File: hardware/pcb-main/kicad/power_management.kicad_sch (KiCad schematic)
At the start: 58 parts, among them J7 TYPE-C-31-M-12, J8 JST_PH_2pin, Q2 PMOS, SW1 SS-12D10L5, U5 BQ24195RGER, U6 TPS61088RHLR, U7 INA219AIDCNR, U8 AMS1117-3.3, U9 USBLC6-2SC6

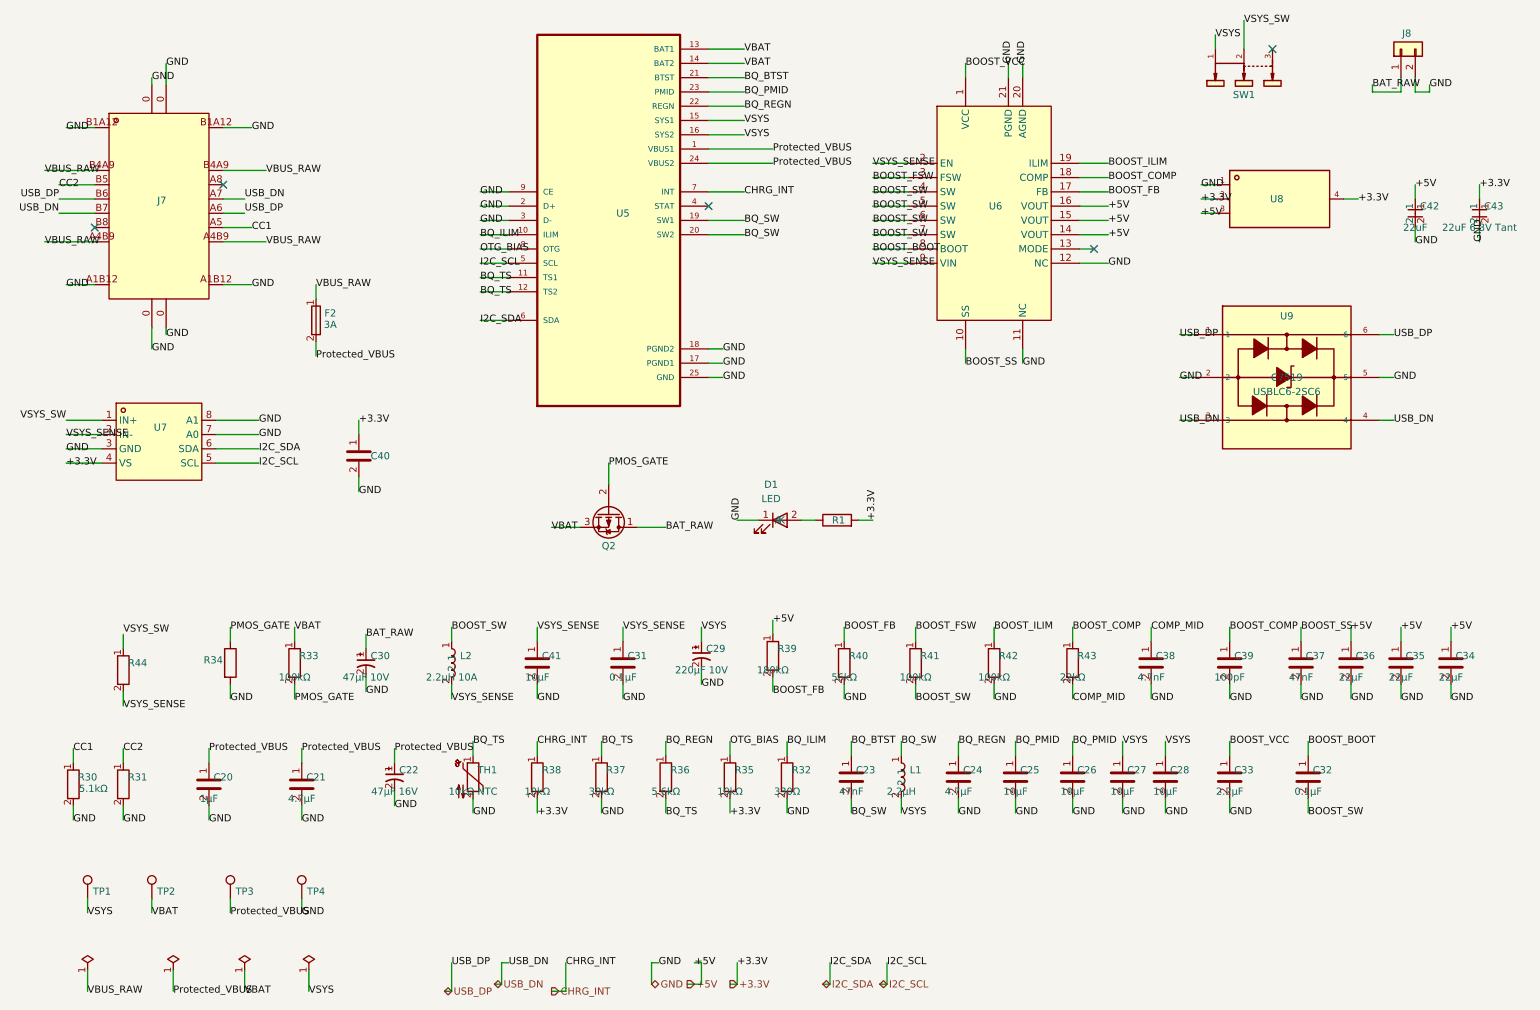
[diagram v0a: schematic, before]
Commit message: Main PCB v7 finalization: schematic, layout, production files, and reports
Includes power management schematic updates, PCB layout changes,
updated BOM/positions/netlist for JLCPCB fabrication, DRC/ERC reports,
slide switch footprint library addition, and review handoff docs.

Co-Authored-By: Claude Opus 4.6 (1M context) <noreply@anthropic.com>
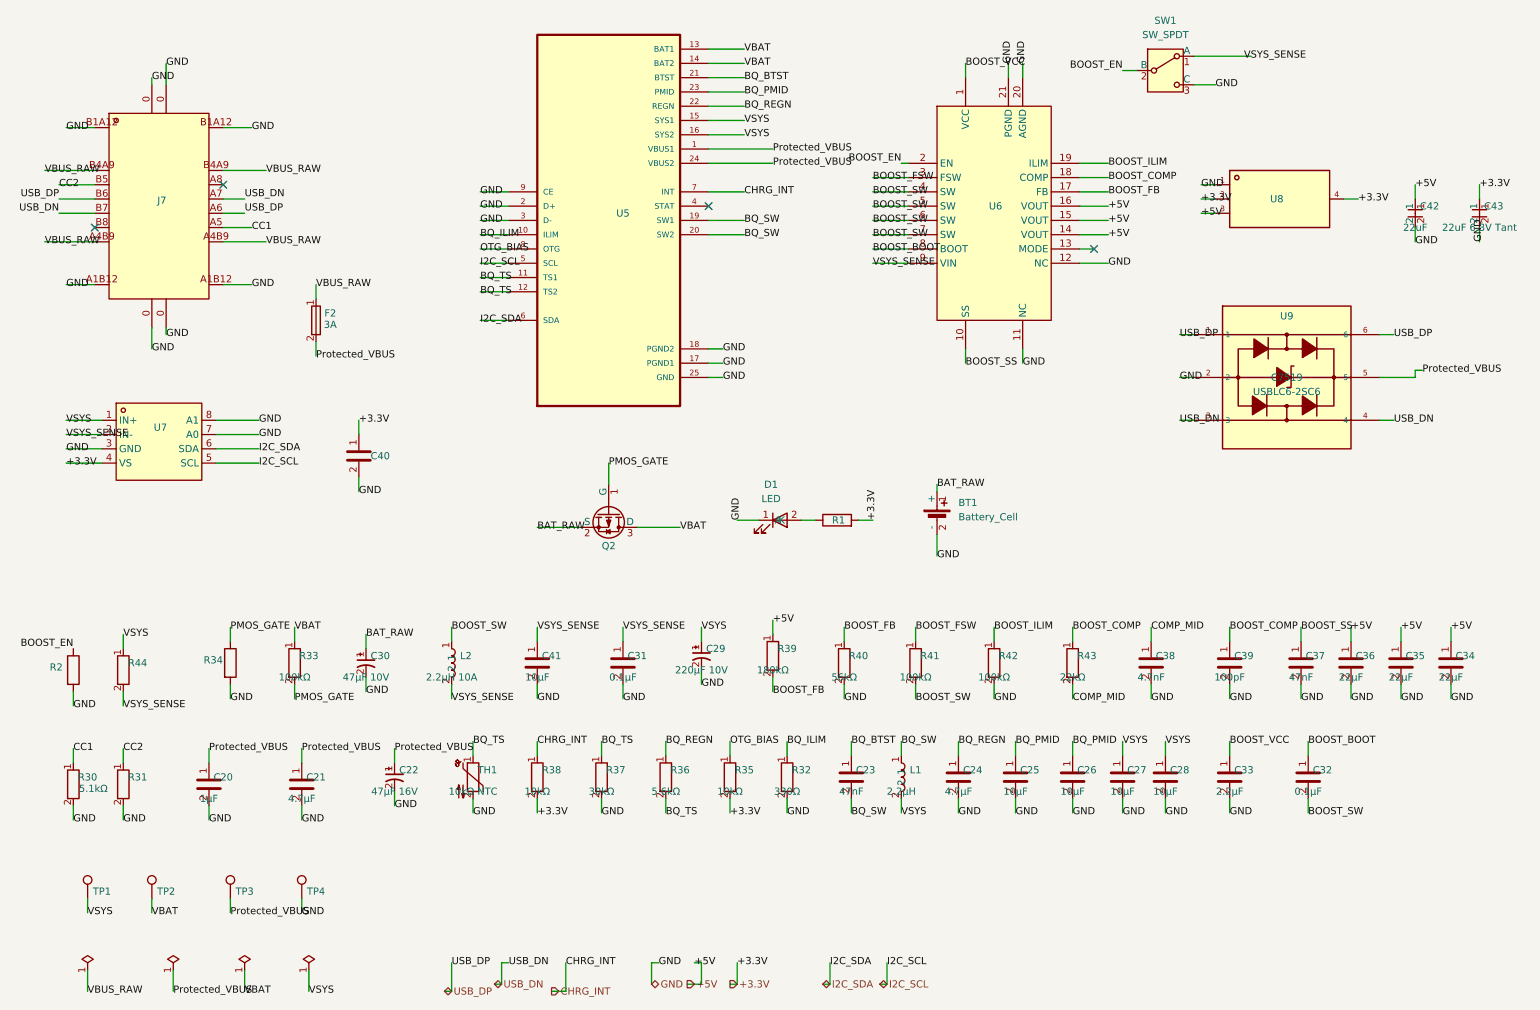
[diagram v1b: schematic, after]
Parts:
- removed J8: JST_PH_2pin, Connector_JST:JST_PH_S2B-PH-SM4-TB_1x02-1MP_P2.00mm_Horizontal, symbol Connector_Generic:Conn_01x02
- removed SW1: SS-12D10L5, JLC-MCP:SW-TH_SS-12D10L5, symbol JLC-MCP-Misc:SS-12D10L5
- added BT1: Battery_Cell, Battery:BatteryHolder_Keystone_1042_1x18650, symbol Device:Battery_Cell
- added R2: 100kΩ, Resistor_SMD:R_0603_1608Metric, symbol Device:R
- added SW1: SW_SPDT, JLC-MCP:MK-12C02-G020_GSW, symbol Switch:SW_SPDT
- Q2: symbol Simulation_SPICE:PMOS -> Transistor_FET:Q_PMOS_GSD
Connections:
- net VSYS_SW is gone; now on net VSYS: R44.1, U7.1 (IN+)
- net BAT_RAW: now also Q2.2 (S), BT1.1 (+); no longer Q2.1 (D)
- net GND: now also BT1.2 (-), R2.2, SW1.3 (C); no longer U9.5
- net PMOS_GATE: now also Q2.1 (G); no longer Q2.2 (G)
- net Protected_VBUS: now also U9.5
- net VSYS_SENSE: now also SW1.1 (A); no longer U6.2 (EN)
- new net BOOST_EN: R2.1, SW1.2 (B), U6.2 (EN)
- no-connect marks 5 -> 4
